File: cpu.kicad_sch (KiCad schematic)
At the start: 10 parts, among them U1 Intel_8088, U2 8087, U3 8284, Y1 14.31818 MHz

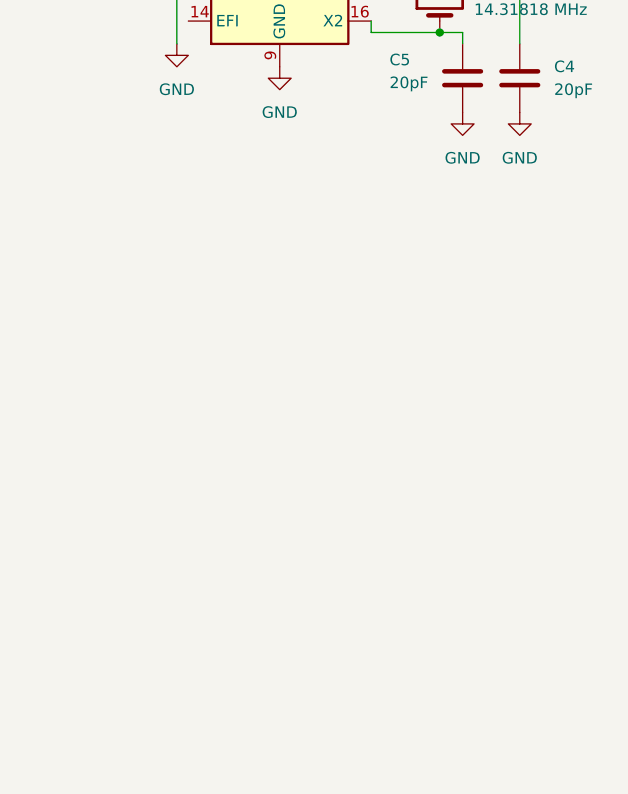
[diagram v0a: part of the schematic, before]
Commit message: Add Bus 8288 controller
Signed-off-by: Lucy Mielke <user@domain.tld>
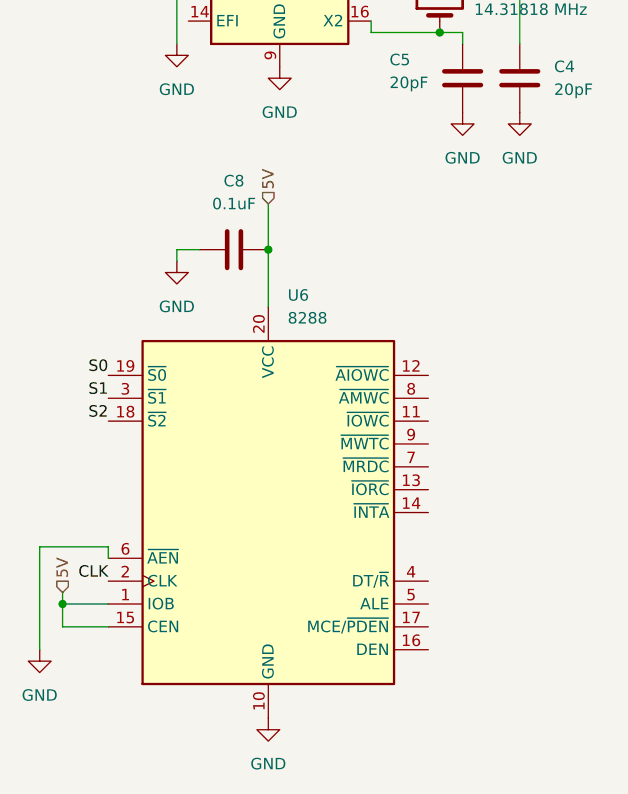
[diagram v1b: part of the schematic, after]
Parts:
- added C8: 0.1uF, Capacitor_THT:C_Disc_D3.0mm_W1.6mm_P2.50mm, symbol Device:C
- added U6: 8288, Package_DIP:DIP-20_W7.62mm_Socket, symbol Interface:8288
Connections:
- net 5V: now also C8.2, U6.1 (IOB), U6.15 (CEN), U6.20 (VCC)
- net CLK: now also U6.2 (CLK)
- net GND: now also C8.1, U6.10 (GND), U6.6 (~{AEN})
- net S0: now also U6.19 (~{S0})
- net S1: now also U6.3 (~{S1})
- net S2: now also U6.18 (~{S2})

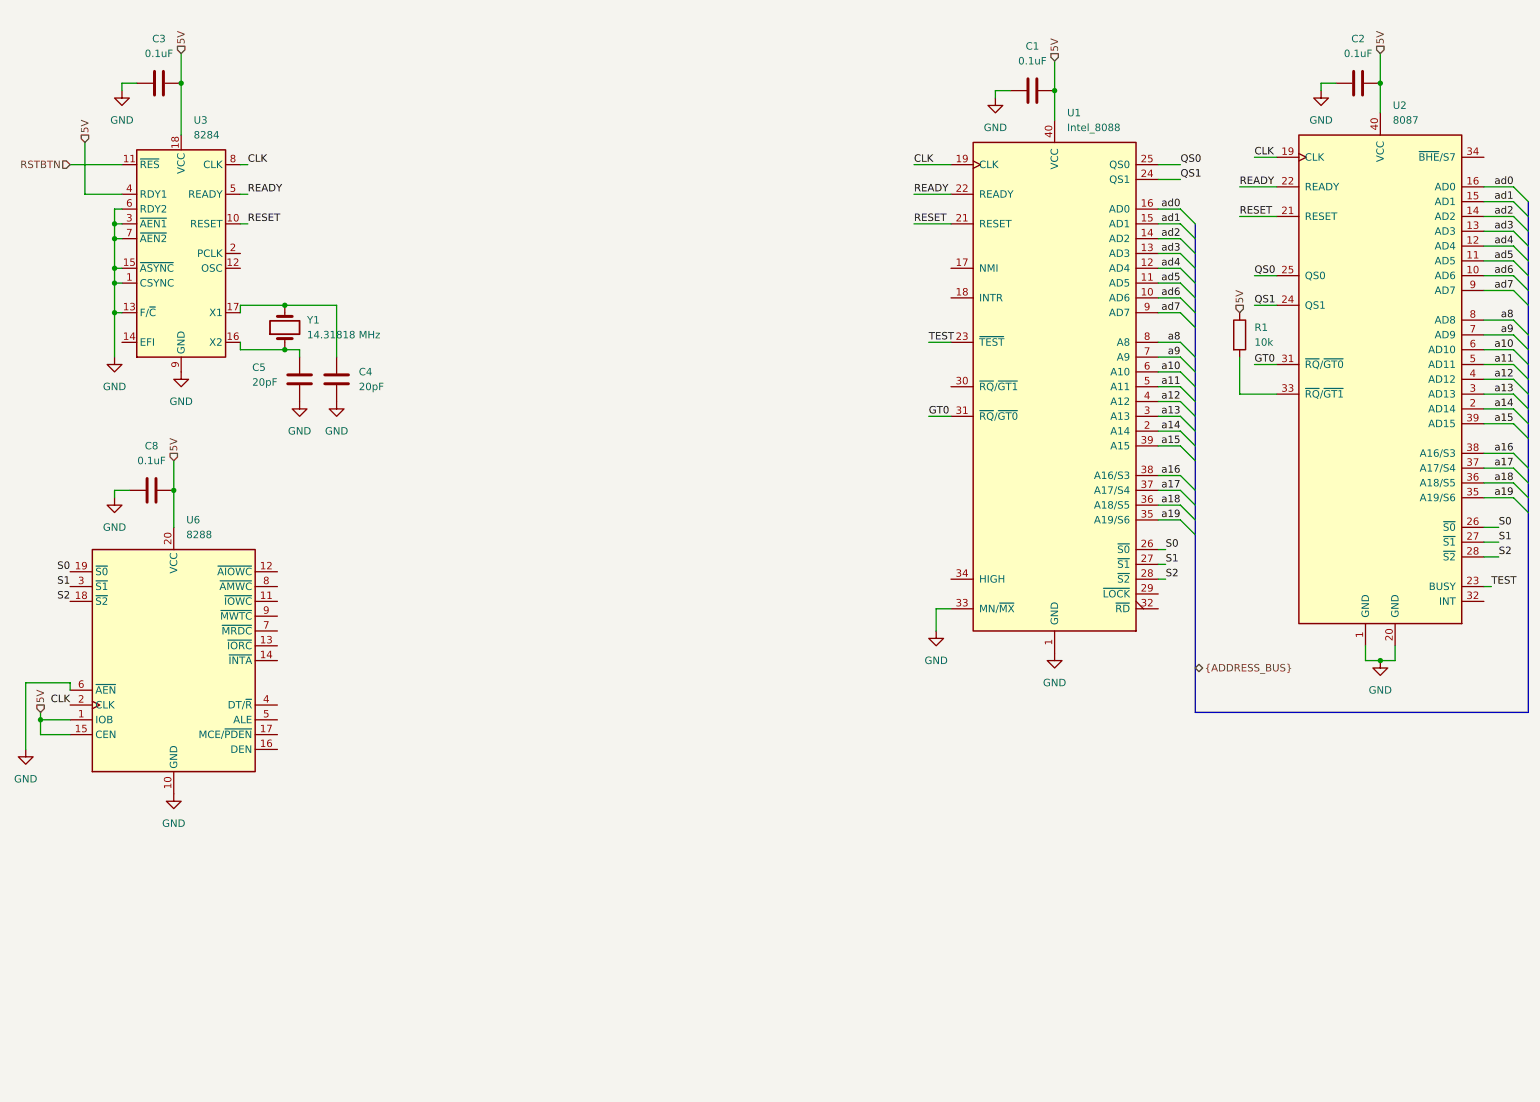
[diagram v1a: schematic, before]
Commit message: Memory mapping for RAM and ROM (BIOS)
Signed-off-by: Lucy Mielke <user@domain.tld>
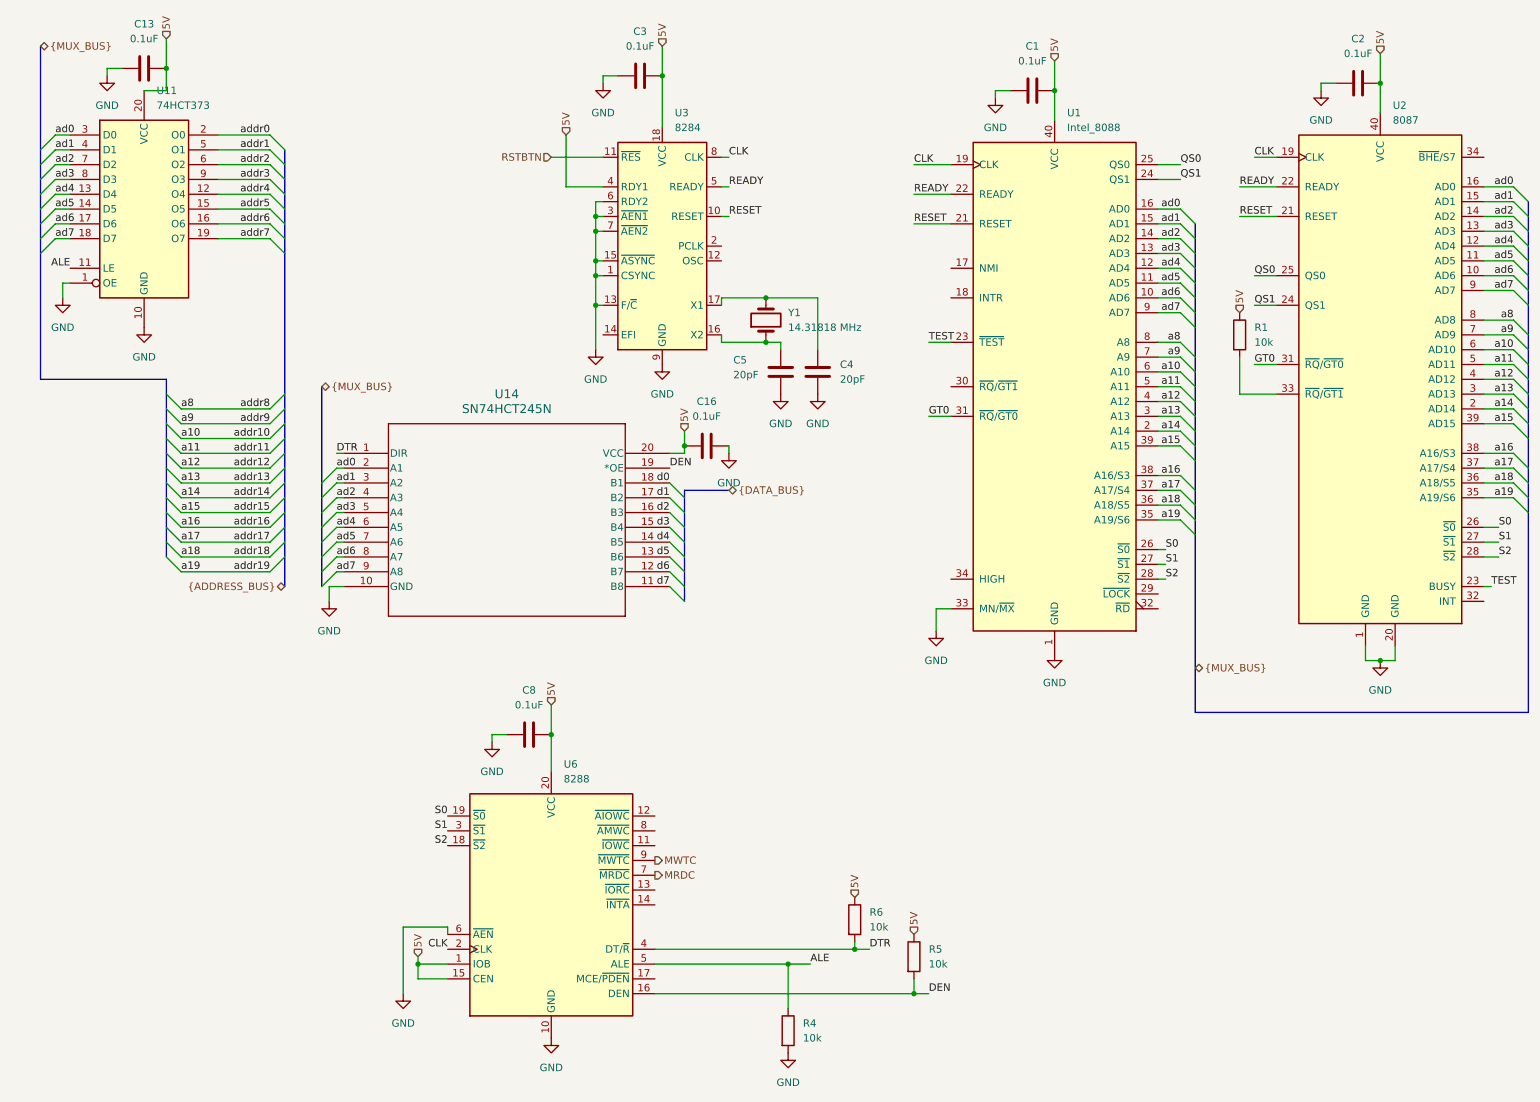
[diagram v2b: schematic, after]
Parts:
- added C13, C16: 0.1uF, Capacitor_THT:C_Disc_D3.0mm_W1.6mm_P2.50mm, symbol Device:C
- added R4, R5, R6: 10k, Resistor_THT:R_Axial_DIN0204_L3.6mm_D1.6mm_P5.08mm_Horizontal, symbol Device:R
- added U11: 74HCT373, Package_DIP:DIP-20_W7.62mm_Socket, symbol 74xx:74HCT373
- added U14: SN74HCT245N, SN74HCT245N Transciever:SN74HCT245N, symbol SN74HCT245N:SN74HCT245N
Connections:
- net 5V: now also C13.2, C16.2, R5.1, R6.1, U11.20 (VCC), U14.20 (VCC)
- net GND: now also C13.1, C16.1, R4.2, U11.1 (OE), U11.10 (GND), U14.10 (GND)
- net ad0: now also U11.3 (D0), U14.2 (A1)
- net ad1: now also U11.4 (D1), U14.3 (A2)
- net ad2: now also U11.7 (D2), U14.4 (A3)
- net ad3: now also U11.8 (D3), U14.5 (A4)
- net ad4: now also U11.13 (D4), U14.6 (A5)
- net ad5: now also U11.14 (D5), U14.7 (A6)
- net ad6: now also U11.17 (D6), U14.8 (A7)
- net ad7: now also U11.18 (D7), U14.9 (A8)
- net DEN: now reaches U6.16 (DEN)
- net DEN: now also R5.2, U14.19 (*OE)
- net DTR: now reaches U6.4 (DT/~{R})
- net DTR: now also R6.2, U14.1 (DIR)
- net ALE: now reaches U6.5 (ALE)
- net ALE: now also R4.1, U11.11 (LE)
- net MRDC: now reaches U6.7 (~{MRDC})
- net MWTC: now reaches U6.9 (~{MWTC})
- new net addr0: U11.2 (O0)
- new net addr1: U11.5 (O1)
- new net addr2: U11.6 (O2)
- new net addr3: U11.9 (O3)
- new net addr4: U11.12 (O4)
- new net addr5: U11.15 (O5)
- new net addr6: U11.16 (O6)
- new net addr7: U11.19 (O7)
- new net d0: U14.18 (B1)
- new net d1: U14.17 (B2)
- new net d2: U14.16 (B3)
- new net d3: U14.15 (B4)
- new net d4: U14.14 (B5)
- new net d5: U14.13 (B6)
- new net d6: U14.12 (B7)
- new net d7: U14.11 (B8)
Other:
- moved on the sheet: C3, C4, C5, C8, U3, U6, Y1

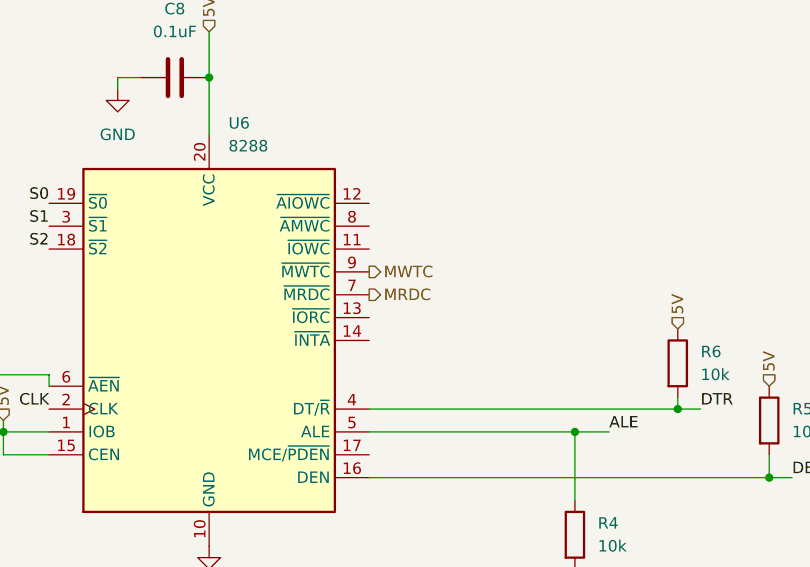
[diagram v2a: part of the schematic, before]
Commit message: Complete UART connection
Signed-off-by: Lucy Mielke <user@domain.tld>
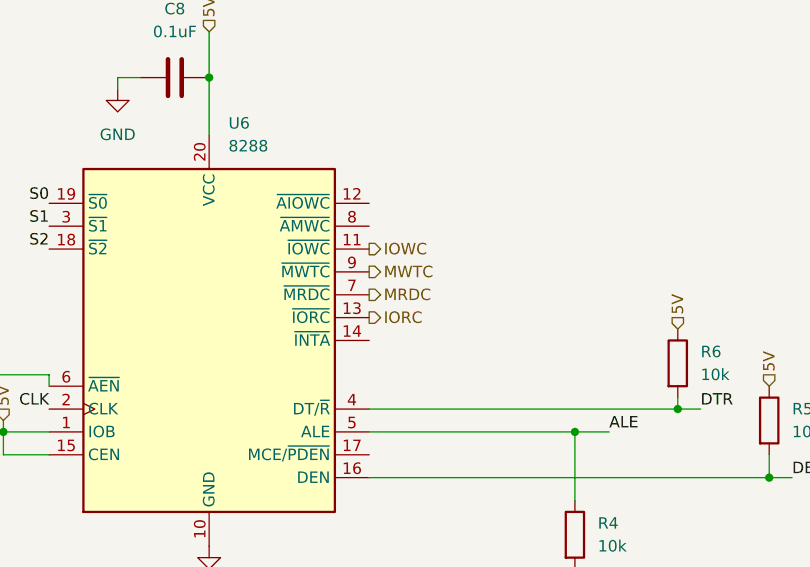
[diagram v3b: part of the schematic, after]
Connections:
- net IOWC: now reaches U6.11 (~{IOWC})
- net IORC: now reaches U6.13 (~{IORC})
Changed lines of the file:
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@@
+		)
+	)
+	(hierarchical_label "IOWC"
+		(shape output)
+		(at 123.19 154.94 0)
+		(effects
+			(font
+				(size 1.27 1.27)
+			)
+			(justify left)
 		)
 	)
@@
 		)
 	)
+	(hierarchical_label "IORC"
+		(shape output)
+		(at 123.19 162.56 0)
+		(effects
+			(font
+				(size 1.27 1.27)
+			)
+			(justify left)
+		)
+	)

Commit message: PIC controller added
Signed-off-by: Lucy Mielke <user@domain.tld>
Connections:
- net INTR: now reaches U1.18 (INTR)
- net INTA: now reaches U6.14 (~{INTA})
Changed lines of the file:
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@@
+		)
+	)
+	(hierarchical_label "INTA"
+		(shape input)
+		(at 123.19 165.1 0)
+		(effects
+			(font
+				(size 1.27 1.27)
+			)
+			(justify left)
 		)
 	)
@@
 		)
 	)
+	(hierarchical_label "INTR"
+		(shape output)
+		(at 173.99 60.96 180)
+		(effects
+			(font
+				(size 1.27 1.27)
+			)
+			(justify right)
+		)
+	)

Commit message: reorganise
Signed-off-by: Lucy Mielke <user@domain.tld>
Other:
- note added: "Compute (CPU/FPU/Bus demux/System clock)"
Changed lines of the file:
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@@
 		(comment 1 "${COMMENT1}")
+	)
+	(text "Compute\n(CPU/FPU/Bus demux/System clock)"
+		(exclude_from_sim no)
+		(at 154.94 18.288 0)
+		(effects
+			(font
+				(size 1.905 1.905)
+			)
+		)
 	)
 	(junction

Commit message: add PIT
Signed-off-by: Lucy Mielke <user@domain.tld>
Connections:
- net PCLK: now reaches U3.2 (PCLK)
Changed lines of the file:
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@@
+		)
+	)
+	(hierarchical_label "PCLK"
+		(shape output)
+		(at 134.62 52.07 0)
+		(effects
+			(font
+				(size 1.27 1.27)
+			)
+			(justify left)
 		)
 	)

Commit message: IDE controller/connector
Signed-off-by: Lucy Mielke <user@domain.tld>
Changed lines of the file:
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@@
-		)
-	)
-	(label "DTR"
-		(at 68.58 87.63 0)
-		(effects
-			(font
-				(size 1.27 1.27)
-			)
-			(justify left bottom)
 		)
 	)
@@
 			)
 			(justify right bottom)
-		)
-	)
-	(label "DTR"
-		(at 160.02 172.72 0)
-		(effects
-			(font
-				(size 1.27 1.27)
-			)
-			(justify left bottom)
 		)
 	)
@@
 		)
 	)
+	(hierarchical_label "DTR"
+		(shape input)
+		(at 68.58 87.63 180)
+		(effects
+			(font
+				(size 1.27 1.27)
+			)
+			(justify right)
+		)
+	)
 	(hierarchical_label "MRDC"
 		(shape output)
@@
 		(effects
 			(font
+				(size 1.27 1.27)
+			)
+			(justify left)
+		)
+	)
+	(hierarchical_label "DTR"
+		(shape input)
+		(at 160.02 172.72 0)
+		(effects
+			(font

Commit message: ISA card slots, schematic cleanup
Signed-off-by: Lucy Mielke <user@domain.tld>
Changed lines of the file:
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@@
-		)
-	)
-	(label "CLK"
-		(at 167.64 38.1 0)
-		(effects
-			(font
-				(size 1.27 1.27)
-			)
-			(justify left bottom)
 		)
 	)
@@
 		)
 	)
-	(label "CLK"
-		(at 226.06 36.83 0)
-		(effects
-			(font
-				(size 1.27 1.27)
-			)
-			(justify left bottom)
-		)
-	)
 	(label "d4"
 		(at 125.73 102.87 180)
@@
 		)
 	)
-	(label "ALE"
-		(at 22.86 55.88 180)
-		(effects
-			(font
-				(size 1.27 1.27)
-			)
-			(justify right bottom)
-		)
-	)
 	(label "ad7"
 		(at 213.36 63.5 180)
@@
 		)
 	)
-	(label "ALE"
-		(at 149.86 175.26 0)
-		(effects
-			(font
-				(size 1.27 1.27)
-			)
-			(justify left bottom)
-		)
-	)
 	(label "a10"
 		(at 41.91 85.09 0)
@@
 	(label "S2"
 		(at 267.97 105.41 0)
-		(effects
-			(font
-				(size 1.27 1.27)
-			)
-			(justify left bottom)
-		)
-	)
-	(label "CLK"
-		(at 135.89 36.83 0)
 		(effects
 			(font
@@
 		)
 	)
+	(hierarchical_label "ALE"
+		(shape input)
+		(at 149.86 175.26 0)
+		(effects
+			(font
+				(size 1.27 1.27)
+			)
+			(justify left)
+		)
+	)
 	(hierarchical_label "MRDC"
 		(shape output)
@@
 		)
 	)
+	(hierarchical_label "CLK"
+		(shape output)
+		(at 167.64 38.1 180)
+		(effects
+			(font
+				(size 1.27 1.27)
+			)
+			(justify right)
+		)
+	)
+	(hierarchical_label "ALE"
+		(shape input)
+		(at 22.86 55.88 180)
+		(effects
+			(font
+				(size 1.27 1.27)
+			)
+			(justify right)
+		)
+	)
 	(hierarchical_label "5V"
 		(shape input)
@@
 		(shape input)
 		(at 160.02 172.72 0)
+		(effects
+			(font
+				(size 1.27 1.27)
+			)
+			(justify left)
+		)
+	)
+	(hierarchical_label "CLK"
+		(shape output)
+		(at 135.89 36.83 0)
 		(effects
 			(font
@@
 		(effects
 			(font
+				(size 1.27 1.27)
+			)
+			(justify right)
+		)
+	)
+	(hierarchical_label "CLK"
+		(shape output)
+		(at 226.06 36.83 180)
+		(effects
+			(font
